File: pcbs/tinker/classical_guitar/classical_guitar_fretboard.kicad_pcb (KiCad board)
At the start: 4 copper layers, 157.6 x 154.4 mm, 188 parts, among them Q1 AO3401A, U1 AT42QT1110-A, U2 AT42QT1110-A, U3 AT42QT1110-A, U4 MP2359

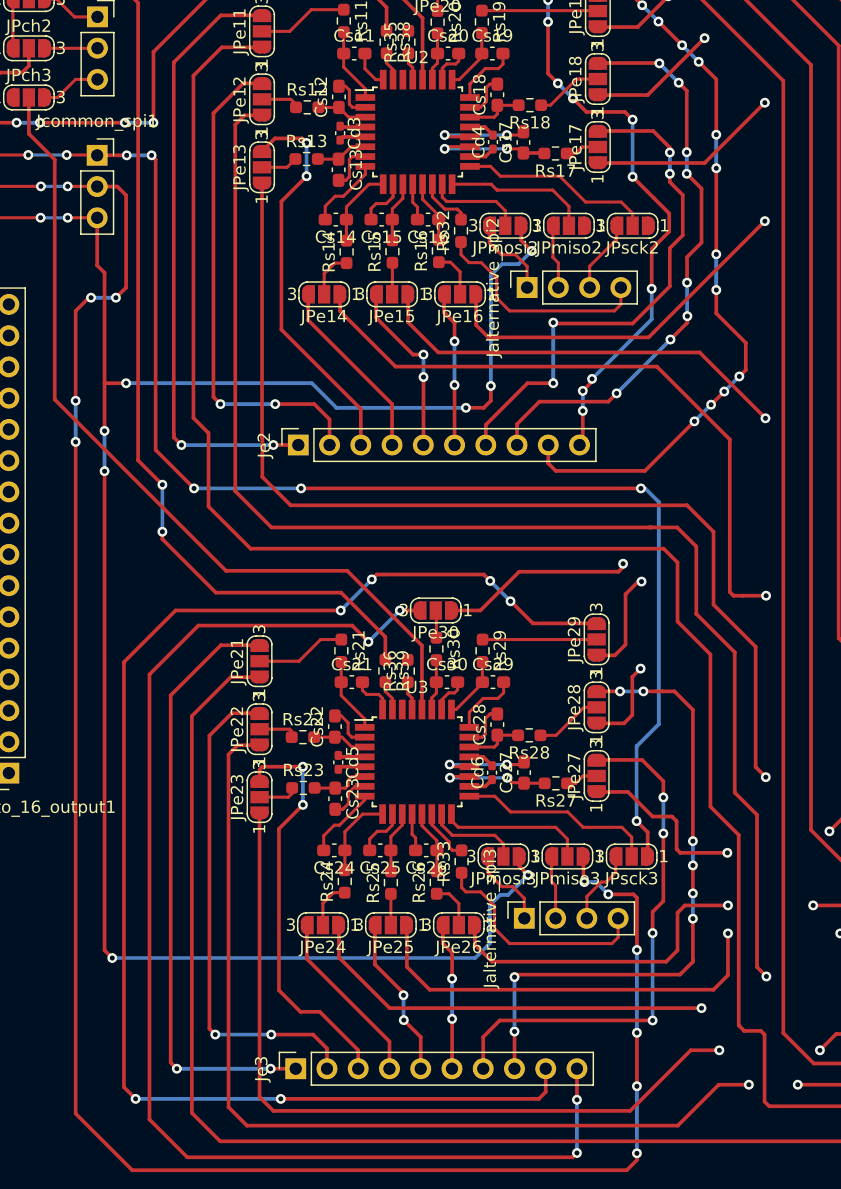
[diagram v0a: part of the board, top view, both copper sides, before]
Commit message: Traces left are VCC and GND
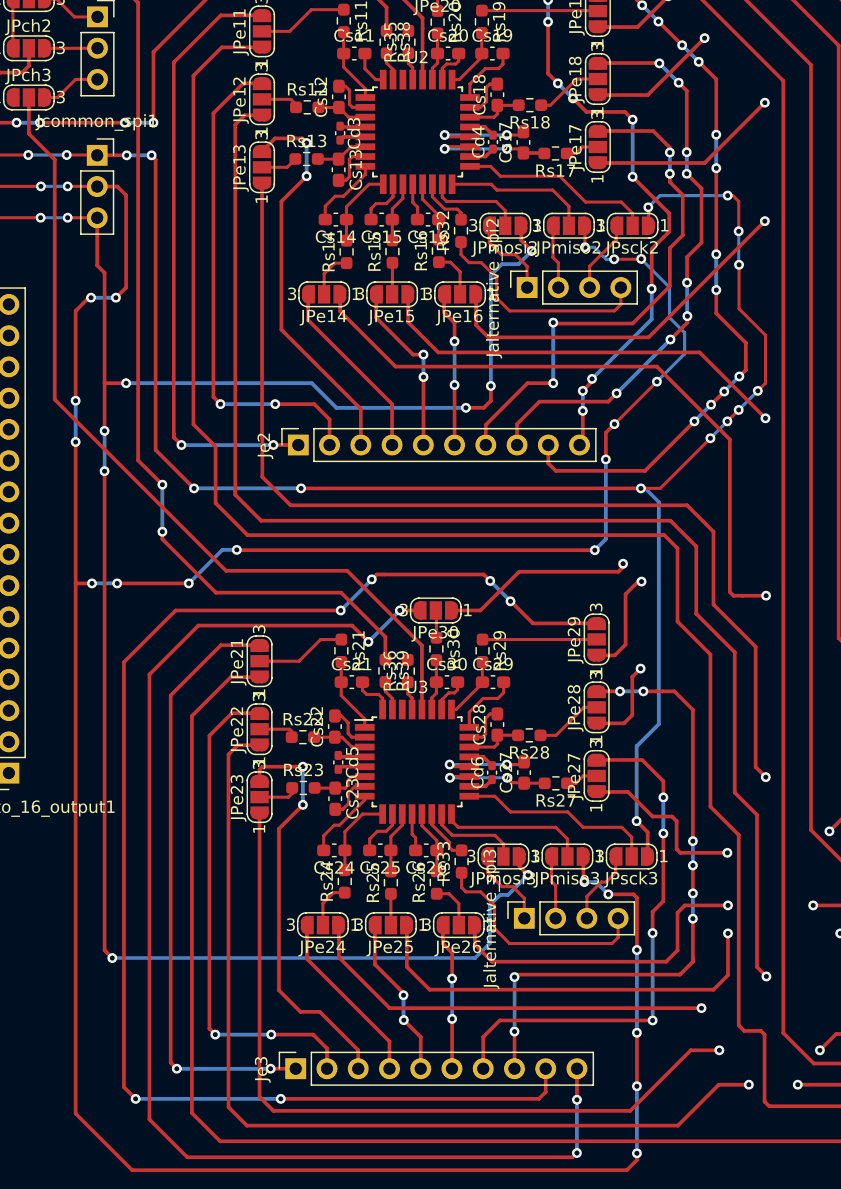
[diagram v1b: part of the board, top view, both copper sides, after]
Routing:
- net /C_MISO: track 275.4 -> 353.6 mm, vias 16 -> 27
- net /C_SCK: track 216.8 -> 255.6 mm, vias 10 -> 18

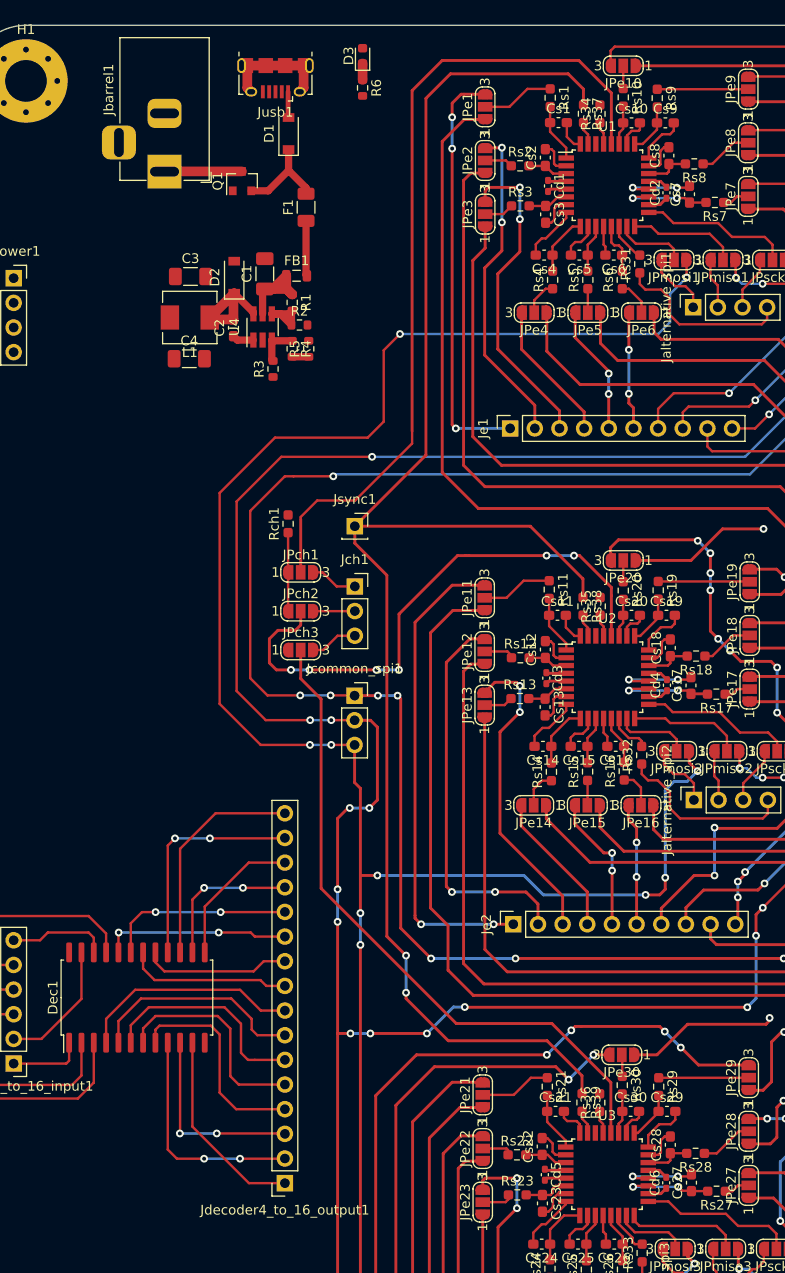
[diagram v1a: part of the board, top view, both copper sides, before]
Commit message: VDD and GND traces added via vias
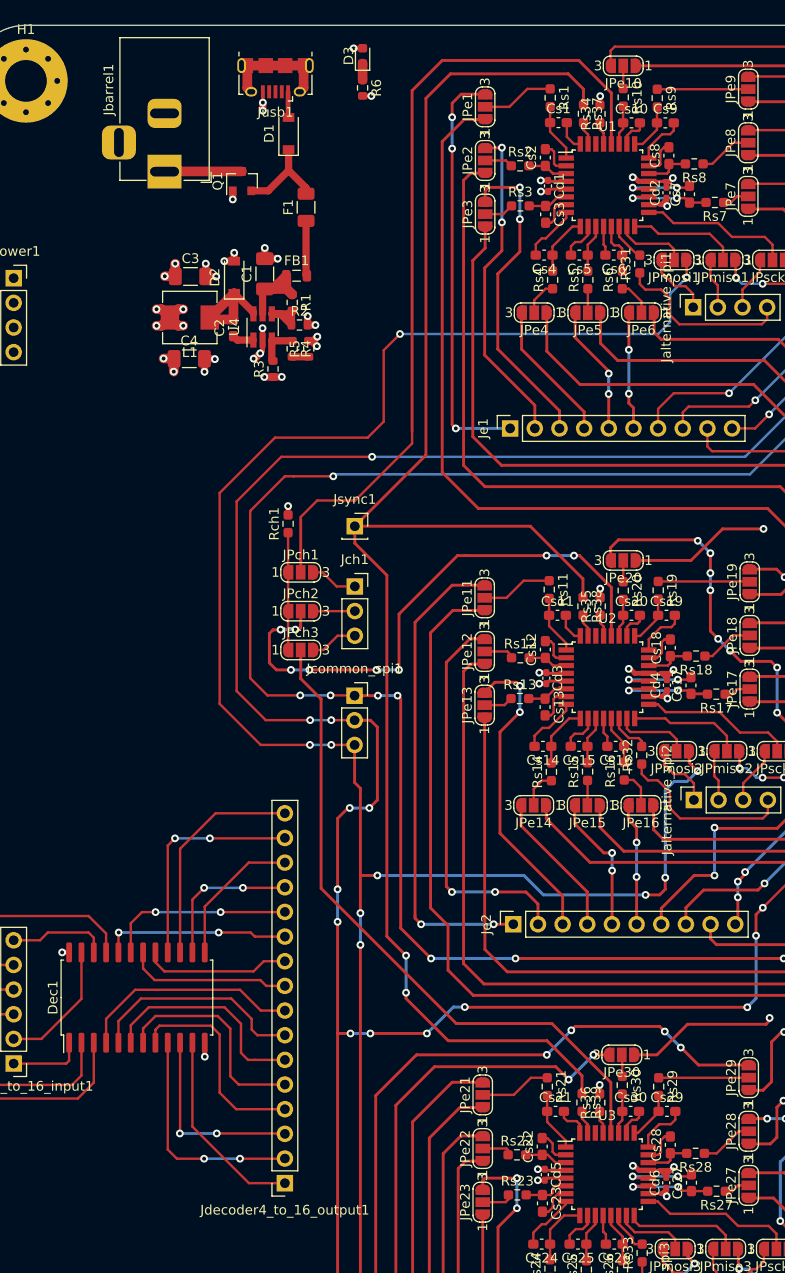
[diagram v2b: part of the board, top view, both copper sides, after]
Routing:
- net GND: track 12.7 -> 50.9 mm, vias 0 -> 29
- net VDD: track 12.5 -> 38.3 mm, vias 0 -> 22
- net Net-(JPch1-Pad1): track 8.09 -> 12.1 mm
- net /Change2: track 57.8 -> 58.3 mm, vias 6 -> 8
